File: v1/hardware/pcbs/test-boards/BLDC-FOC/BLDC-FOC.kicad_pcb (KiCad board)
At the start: 2 copper layers, 100 x 100 mm, 83 parts, among them CN1 HB9500-3, Q1 BSC190N15NS3G(TOKMAS), Q2 BSC190N15NS3G(TOKMAS), Q3 BSC190N15NS3G(TOKMAS), Q4 BSC190N15NS3G(TOKMAS), Q5 BSC190N15NS3G(TOKMAS), Q6 BSC190N15NS3G(TOKMAS)

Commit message: bldc foc test board done
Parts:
- removed BUCK1: LM5164DDA, Package_SO:HSOP-8-1EP_3.9x4.9mm_P1.27mm_EP2.41x3.1mm
- removed L1: PSPMAA0605H-820M-IGF, EasyEDA:IND-SMD_L7.1-W6.6
- added C37: 1uF 200V, Capacitor_SMD:C_1812_4532Metric, F.Cu at (-13.2, 26.1)
- added C38: 1uF 200V, Capacitor_SMD:C_1812_4532Metric, F.Cu at (-38.2, 36.2)
- added C39: 100nF, Capacitor_SMD:C_0603_1608Metric, F.Cu at (-28.0, 5.00)
- added C40: 100nF, Capacitor_SMD:C_0603_1608Metric, F.Cu at (-35.8, 1.00)
- added C41: 4.7nF, Capacitor_SMD:C_0603_1608Metric, F.Cu at (-32.2, -3.60)
- added C5: 1uF 200V, Capacitor_SMD:C_1812_4532Metric, F.Cu at (-21.6, 18.9)
- added C6: 1uF 200V, Capacitor_SMD:C_1812_4532Metric, F.Cu at (-45.8, 36.2)
- added C7: 10uF 25V, Capacitor_SMD:C_0603_1608Metric, F.Cu at (-38.2, 31.6)
- added C8: 100nF 25V, Capacitor_SMD:C_0603_1608Metric, F.Cu at (-35.2, 26.6)
- added D4: SMAJ85CA, Diode_SMD:D_SMA, F.Cu at (-21.6, 22.7)
- added D5: SMAJ15CA, Diode_SMD:D_SMA, F.Cu at (-42.0, 35.6)
- added F1: R1245.100, EasyEDA:FUSE-SMD_L12.5-W4.5, F.Cu at (-14.4, 5.50)
- added J1: Conn_01x12, Connector_JST:JST_XH_S12B-XH-A_1x12_P2.50mm_Horizontal, F.Cu at (-40.0, -4.50)
- added J2: Conn_01x10, Connector_JST:JST_XH_S10B-XH-A_1x10_P2.50mm_Horizontal, F.Cu at (40.0, -20.0)
- added J3: Conn_02x02_Odd_Even, Connector_PinHeader_2.54mm:PinHeader_2x02_P2.54mm_Vertical, F.Cu at (-26.9, -2.33)
- added JP1: Jumper_3_Bridged12, Connector_PinHeader_2.54mm:PinHeader_1x03_P2.54mm_Vertical, F.Cu at (-8.54, -39.0)
- added L2: SL0420-4R7M, EasyEDA:IND-SMD_L4.5-W4.1_IHLP, F.Cu at (-31.4, 26.0)
- added P1: WJ500V-5.08-2P-14-00A, EasyEDA:CONN-TH_2P-P5.00_WJ500V-5.08-2P, F.Cu at (-41.0, 44.0)
- added Q7: SP015N03BGHTO, EasyEDA:TOLL-8_L10.4-W9.9-P1.20-LS11.7-BL, F.Cu at (-12.8, 19.2)
- added Q8: AO3400A_C347475, EasyEDA:SOT-23-3_L2.9-W1.3-P1.90-LS2.4-BR, F.Cu at (-42.6, 28.6)
- added R35: 60, Resistor_SMD:R_0603_1608Metric, F.Cu at (-28.2, -7.60)
- added R36: 60, Resistor_SMD:R_0603_1608Metric, F.Cu at (-28.2, 0.40)
- added R37: 2.7K, Resistor_SMD:R_0603_1608Metric, F.Cu at (-40.3, -44.5)
- added R38: 2.7K, Resistor_SMD:R_0603_1608Metric, F.Cu at (-37.1, -44.5)
- added R39: 2.7K, Resistor_SMD:R_0603_1608Metric, F.Cu at (2.00, -47.3)
- added R40: 2.7K, Resistor_SMD:R_0603_1608Metric, F.Cu at (0.80, -46.1)
- added TP1: TestPoint, Connector_PinSocket_2.54mm:PinSocket_1x01_P2.54mm_Vertical, F.Cu at (36.6, -13.4)
- added TP17: TestPoint, Connector_PinSocket_2.54mm:PinSocket_1x01_P2.54mm_Vertical, F.Cu at (-34.2, -9.20)
- added TP2: TestPoint, Connector_PinSocket_2.54mm:PinSocket_1x01_P2.54mm_Vertical, F.Cu at (32.0, 4.20)
- added TP3: TestPoint, Connector_PinSocket_2.54mm:PinSocket_1x01_P2.54mm_Vertical, F.Cu at (36.6, 27.0)
- added TP4: TestPoint, Connector_PinSocket_2.54mm:PinSocket_1x01_P2.54mm_Vertical, F.Cu at (29.6, -26.8)
- added TP5: TestPoint, Connector_PinSocket_2.54mm:PinSocket_1x01_P2.54mm_Vertical, F.Cu at (-48.0, 45.0)
- added TP6: TestPoint, Connector_PinSocket_2.54mm:PinSocket_1x01_P2.54mm_Vertical, F.Cu at (-8.80, -7.60)
- added TP7: TestPoint, Connector_PinSocket_2.54mm:PinSocket_1x01_P2.54mm_Vertical, F.Cu at (-3.00, -29.4)
- added U2: MX74700T_C22468156, EasyEDA:SOT-23-6_L2.9-W1.6-P0.95-LS2.9-BL, F.Cu at (-21.6, 15.1)
- added U3: KF88SA-16.0-2P, EasyEDA:CONN-TH_KF88SA-16.0-2P, F.Cu at (-17.0, 39.0)
- added U4: MX74700T_C22468156, EasyEDA:SOT-23-6_L2.9-W1.6-P0.95-LS2.9-BL, F.Cu at (-46.0, 30.6)
- added U5: AP63205WU, Package_TO_SOT_SMD:TSOT-23-6, F.Cu at (-38.2, 29.0)
- added U6: AZ1117EH-3.3TRG1, EasyEDA:SOT-223_L6.5-W3.5-P2.30-LS7.0-BR, F.Cu at (-28.4, 12.6)
- added U7: TXS0108EPW, Package_SO:TSSOP-20_4.4x6.5mm_P0.65mm, F.Cu at (-6.00, -45.0)
- added U8: TCAN1057AVDRQ1, EasyEDA:SOIC-8_L4.9-W3.9-P1.27-LS6.0-BL, F.Cu at (-33.0, 5.00)
- C12: value 22uF 100V -> 22uF 25V; footprint Capacitor_SMD:C_Elec_6.3x7.7 -> Capacitor_SMD:C_0805_2012Metric
- C13: value 2.2uF 100V -> 22uF 25V; footprint Capacitor_SMD:C_1210_3225Metric -> Capacitor_SMD:C_0805_2012Metric
- C14: value 2.2nF 50V X7R -> 1uF
- C15: value 47uF 50V -> 1uF; footprint Capacitor_SMD:C_Elec_6.3x7.7 -> Capacitor_SMD:C_0603_1608Metric
- Q1, Q2, Q3, Q4, Q5, Q6: value BSC190N15NS3G(TOKMAS) -> BSC093N15NS5
- R4: value 124K -> 32.4K
- R6: value 448K -> 32.4K
- R7: value 39K -> 10K
- moved C2 166.0 mm to (11.3, -35.2), turned to 180 degrees
- moved C4 153.4 mm to (5.75, 19.2), turned to 180 degrees
- moved C3 153.0 mm to (5.75, 0.40), turned to 180 degrees
- moved C1 140.2 mm to (3.15, -18.2), turned to 180 degrees
- moved C10 133.8 mm to (26.0, -40.0)
- moved C11 133.8 mm to (24.6, -36.2)
- moved C9 133.8 mm to (24.6, -43.8)
- moved D1 133.8 mm to (22.2, -46.0)
- moved D2 133.8 mm to (28.2, -42.4)
- moved D3 133.8 mm to (27.0, -34.0)
- moved GDRV1 133.8 mm to (22.0, -40.0)
- moved R1 107.5 mm to (-11.2, -13.8), turned to 180 degrees
- moved R2 104.7 mm to (-12.0, -16.2), turned to 90 degrees
- moved R3 103.1 mm to (-12.0, -19.4), turned to 90 degrees
- moved C15 99.1 mm to (-25.6, 9.60), turned to 90 degrees
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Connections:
- C12 pad 1: VMOT -> +5V
- C13 pad 1: VMOT -> +5V
- C14 pad 1: Net-(BUCK1-BST) -> +5V
- C14 pad 2: Net-(BUCK1-SW) -> GND
- C15 pad 1: VGATE -> +3V3
- D1 pad 2: VGATE -> +12V
- D2 pad 2: VGATE -> +12V
- D3 pad 2: VGATE -> +12V
- GDRV1 pad 4: VGATE -> +12V
- R4 pad 1: Net-(BUCK1-RON) -> +5V
- R4 pad 2: GND -> /5V_SENSE
- R5 pad 1: /BUCK_PGOOD -> /5V_SENSE
- R5 pad 2: +3V3 -> GND
- R6 pad 1: VGATE -> +12V
- R6 pad 2: Net-(BUCK1-FB) -> /12V_SENSE
- R7 pad 1: Net-(BUCK1-FB) -> /12V_SENSE
- U1 pad 10: unconnected-(U1-PB7-Pad10) -> /USART1_RX
- U1 pad 12: unconnected-(U1-PC13-Pad12) -> /U_LOW_PWM
- U1 pad 13: unconnected-(U1-PA0-Pad13) -> /VMOT_SENSE
- U1 pad 14: unconnected-(U1-NRST-Pad14) -> /NRST
- U1 pad 15: /SK6812_data -> unconnected-(U1-SK6812_data-Pad15)
- U1 pad 16: +3V3 -> unconnected-(U1-3V3-Pad16)
- U1 pad 23: unconnected-(U1-PA9-Pad23) -> /V_HIGH_PWM
- U1 pad 24: unconnected-(U1-PA8-Pad24) -> /U_HIGH_PWM
- U1 pad 25: unconnected-(U1-PB14-Pad25) -> /V_LOW_PWM
- U1 pad 26: unconnected-(U1-PB13-Pad26) -> /FDCAN2_TX
- U1 pad 27: unconnected-(U1-PB12-Pad27) -> /FDCAN2_RX
- U1 pad 28: unconnected-(U1-PB11-Pad28) -> /SHIFTER_OE
- U1 pad 29: unconnected-(U1-PB2-Pad29) -> /CAN_SILENT
- U1 pad 3: unconnected-(U1-PA10-Pad3) -> /W_HIGH_PWM
- U1 pad 30: unconnected-(U1-PB1-Pad30) -> /W_LOW_PWM
- U1 pad 31: unconnected-(U1-PB0-Pad31) -> /V_I_SENSE
- U1 pad 32: unconnected-(U1-PA7-Pad32) -> /W_I_SENSE
- U1 pad 33: unconnected-(U1-PA6-Pad33) -> /12V_SENSE
- U1 pad 34: unconnected-(U1-PA5-Pad34) -> /5V_SENSE
- U1 pad 35: unconnected-(U1-PA4-Pad35) -> /SPI1_SCS
- U1 pad 36: unconnected-(U1-PA3-Pad36) -> /USART2_RX
- U1 pad 37: GND -> /USART2_TX
- U1 pad 38: +5V -> /U_I_SENSE
- U1 pad 4: unconnected-(U1-PB9-Pad4) -> /I2C1_SDA
- U1 pad 41: (no net) -> unconnected-(U1-H1-Pad41)_2
- U1 pad 42: (no net) -> unconnected-(U1-H2-Pad42)_2
- U1 pad 43: (no net) -> unconnected-(U1-H3-Pad43)_4
- U1 pad 5: unconnected-(U1-PA15-Pad5) -> /I2C1_SCL
- U1 pad 6: unconnected-(U1-PB3-Pad6) -> /SPI1_SCLK
- U1 pad 7: unconnected-(U1-PB4-Pad7) -> /SPI1_MISO
- U1 pad 8: unconnected-(U1-PB5-Pad8) -> /SPI1_MOSI
- U1 pad 9: unconnected-(U1-PB6-Pad9) -> /USART1_TX
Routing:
- net +5V: track 0.00 -> 223.3 mm
- net +12V: track 0.00 -> 186.8 mm, vias 0 -> 12
- net /W_I_SENSE: track 4.49 -> 123.7 mm, vias 0 -> 1
- net /V_I_SENSE: track 4.49 -> 93.6 mm, vias 0 -> 1
- net /U_LOW_PWM: track 2.00 -> 85.6 mm, vias 0 -> 1
- net ENC_VCC: track 0.00 -> 79.8 mm
- net /W_HIGH_PWM: track 2.66 -> 81.6 mm, vias 0 -> 2
- net +3V3: track 14.5 -> 89.1 mm, vias 0 -> 23
- net /U_I_SENSE: track 4.49 -> 72.5 mm, vias 0 -> 1
- net /W_LOW_GATE: track 12.8 -> 80.6 mm, vias 0 -> 2
- net GND: track 168.2 -> 234.5 mm, vias 132 -> 147
- net /W_HIGH_GATE: track 20.3 -> 79.9 mm, vias 0 -> 2
- net /USART1_RX_ENC: track 0.00 -> 58.7 mm, vias 0 -> 1
- net /USART1_TX_ENC: track 0.00 -> 56.8 mm, vias 0 -> 1
- net /SPI1_SCS_ENC: track 0.00 -> 54.6 mm, vias 0 -> 1
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- added copper zone on In1.Cu, net +3V3
- added copper zone on F.Cu, net /power/VMOT_UNFILTERED
- added copper zone on F.Cu, net /power/VMOT_UNFUSED
- added copper zone on In2.Cu, net GND
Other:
- outline, holes or cut-outs redrawn
- copper layers 2 -> 4
- board text added: "100nF 25V"
- board text added: "10uF 25V"
- board text added: "12V GND"
- board text added: "1uF"
- board text added: "2.7K"
- board text added: "22uF 25V"
- board text added: "32.4K"
- board text added: "3PHASE POWER"
- board text added: "3V3"
- board text added: "4.7nF"
- board text added: "5V"
- board text added: "60"
- board text added: "AO3400A"
- board text added: "AP63205WU"
- board text added: "AZ1117EH -3.3TRG1"
- board text added: "BOOT0"
- board text added: "CAN +"
- board text added: "CAN -"
- board text added: "CAN+"
- board text added: "CAN-"
- board text added: "CAN_TERM"
- board text added: "ENCODER"
- board text added: "ENC_VCC"
- board text added: "GND"
- board text added: "KF88SA-16.0-2P"
- board text added: "MISO/GP"
- board text added: "MOSI/GP"
- board text added: "MX74700T"
- board text added: "NRST"
- board text added: "R1245.100"
- board text added: "RX/GP"
- board text added: "SCL"
- board text added: "SCLK/GP"
- board text added: "SCS/GP"
- board text added: "SDA"
- board text added: "SL0420 -4R7M"
- board text added: "SMAJ85CA"
- board text added: "SP015N03BGHTO"
- board text added: "TCAN1057AVDRQ1"
- board text added: "TX/GP"
- board text added: "TXS0108EPW"
- board text added: "U"
- board text added: "UART_RX"
- board text added: "UART_TX"
- board text added: "V"
- board text added: "VMOT"
- board text added: "W"
- board text added: "WJ500V-5.08 -2P-14-00A"
- board text removed: "124K"
- board text removed: "2.2nF 50V X7R"
- board text removed: "2.2uF 100V"
- board text removed: "22uF 100V"
- board text removed: "39K"
- board text removed: "448K"
- board text removed: "47uF 50V"
- board text removed: "82uH I_sat >= 1.6A PSPMAA0605H -820M-IGF"
- board text removed: "LM5164DDA"

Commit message: flooded ground
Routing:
- added copper zone on B.Cu, net GND
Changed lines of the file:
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@@
+	)
+	(zone
+		(net 71)
+		(net_name "GND")
+		(layers "F.Cu" "B.Cu" "In2.Cu")
+		(hatch edge 0.5)
+		(connect_pads yes
+			(clearance 0.5)
+		)
+		(min_thickness 0.25)
+		(filled_areas_thickness no)
+		(fill yes
+			(thermal_gap 0.5)
+			(thermal_bridge_width 0.5)
+		)
+		(polygon
+			(pts
+				(xy -51 -51) (xy 51 -51) (xy 51 51) (xy -51 51)
+			)
+		)
 	)
 	(zone
@@
 			)
 		)
-	)
-	(zone
-		(net 71)
-		(net_name "GND")
-		(layer "In2.Cu")
-		(hatch edge 0.5)
-		(priority 1)
-		(connect_pads yes
-			(clearance 0.5)
-		)
-		(min_thickness 0.25)
-		(filled_areas_thickness no)
-		(fill yes
-			(thermal_gap 0.5)
-			(thermal_bridge_width 0.5)
-		)
-		(polygon
-			(pts
-				(xy -51 -51) (xy 51 -51) (xy 51 51) (xy -51 51)
-			)
-		)

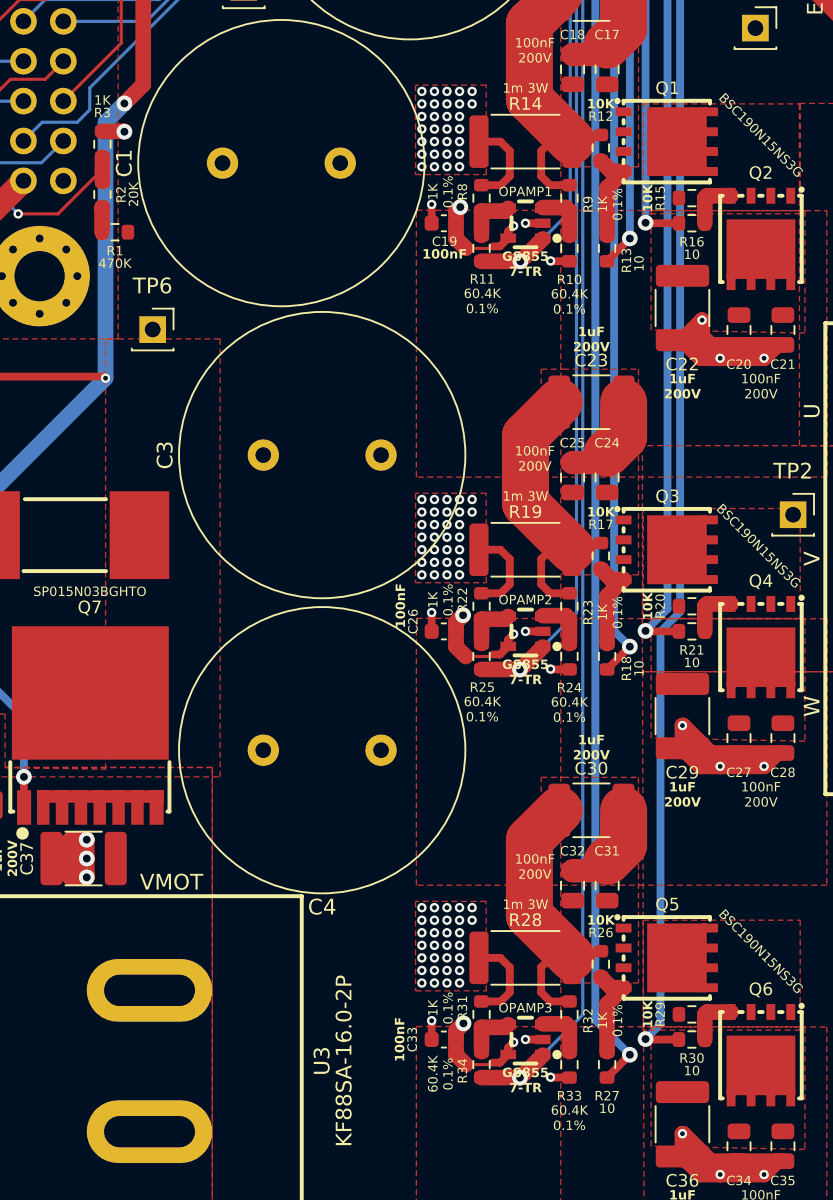
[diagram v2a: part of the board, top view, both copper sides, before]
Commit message: larger resistors for high voltages, new prod files
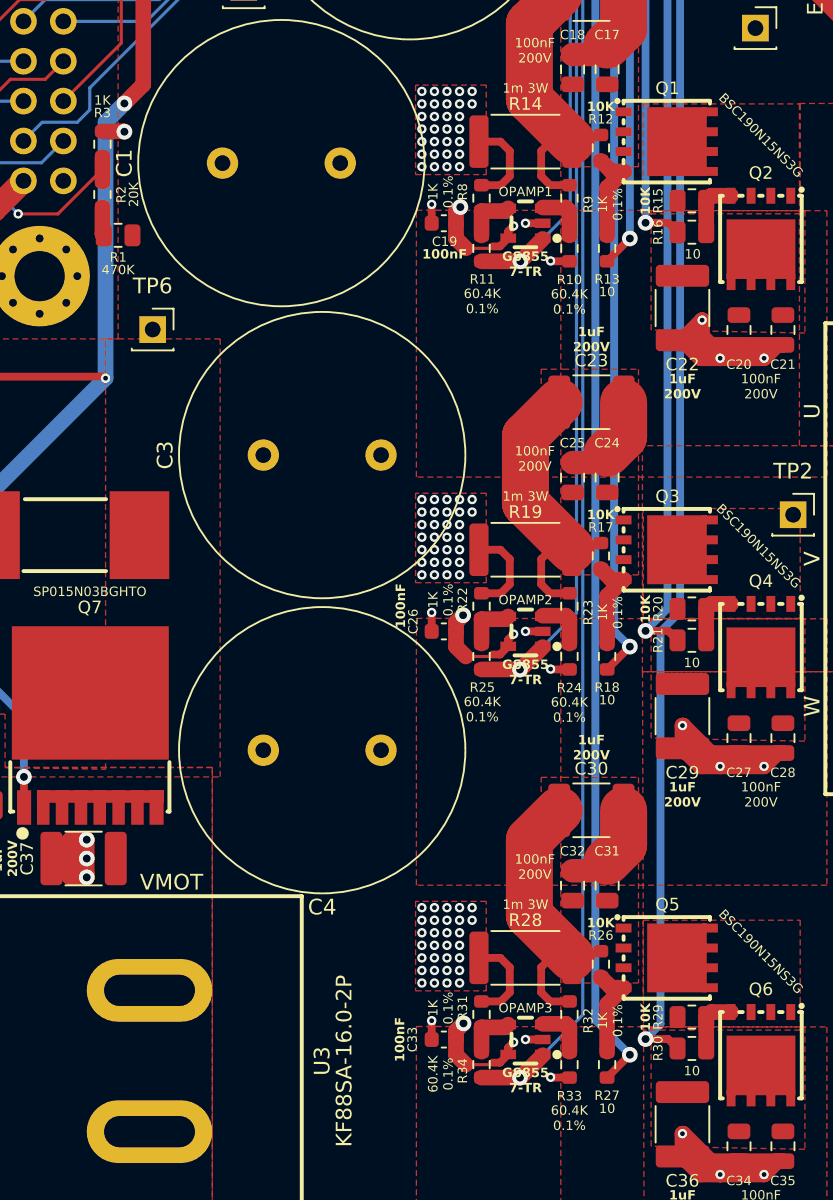
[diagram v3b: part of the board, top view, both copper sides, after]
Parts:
- C1, C2, C3, C4: value 470uF 100V (C443161) -> 820uF 100V (C443165)
- R1, R15, R16, R20, R21, R29, R30: footprint Resistor_SMD:R_0603_1608Metric -> Resistor_SMD:R_0805_2012Metric
- moved R16 0.57 mm to (25.6, -13.8)
- moved R30 0.57 mm to (25.6, 38.2)
- moved R21 0.57 mm to (25.6, 12.2)
- moved R1 0.28 mm to (-11.0, -13.6)
- moved R15 0.17 mm to (25.6, -15.8)
- moved R29 0.17 mm to (25.6, 36.2)
- moved R20 0.17 mm to (25.6, 10.2)

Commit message: new FOC driver schematic
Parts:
- C1, C2, C3, C4: footprint Capacitor_THT:C_Radial_D18.0mm_H35.5mm_P7.50mm -> footprints:C_Radial_D18.0mm_H35.5mm_P7.50mm
- C10, C11, C12, C13, C17, C18, C20, C21, C24, C25, C27, C28, C31, C32, C34, C35, C9: footprint Capacitor_SMD:C_0805_2012Metric -> footprints:C_0805_2012Metric
- C14, C15, C19, C26, C33, C39, C40, C41, C7, C8: footprint Capacitor_SMD:C_0603_1608Metric -> footprints:C_0603_1608Metric
- C16, C22, C23, C29, C30, C36, C37, C38, C5, C6: footprint Capacitor_SMD:C_1812_4532Metric -> footprints:C_1812_4532Metric
- CN1: footprint EasyEDA:CONN-TH_3P-P9.50_HB9500-9.5-3P -> footprints:CONN-TH_3P-P9.50_HB9500-9.5-3P
- D1, D2, D3: value B5819W -> C7420332; footprint Diode_SMD:D_SOD-123F -> footprints:D_SOD-123F
- D4, D5: footprint Diode_SMD:D_SMA -> footprints:D_SMA
- F1: footprint EasyEDA:FUSE-SMD_L12.5-W4.5 -> footprints:FUSE-SMD_L12.5-W4.5
- GDRV1: footprint Snapeda:FD6288Q_QFN50P400X400X90-25N -> footprints:FD6288Q_QFN50P400X400X90-25N
- J1: footprint Connector_JST:JST_XH_S12B-XH-A_1x12_P2.50mm_Horizontal -> footprints:JST_XH_S12B-XH-A_1x12_P2.50mm_Horizontal
- J2: footprint Connector_JST:JST_XH_S10B-XH-A_1x10_P2.50mm_Horizontal -> footprints:JST_XH_S10B-XH-A_1x10_P2.50mm_Horizontal
- J3: footprint Connector_PinHeader_2.54mm:PinHeader_2x02_P2.54mm_Vertical -> footprints:PinHeader_2x02_P2.54mm_Vertical
- JP1: footprint Connector_PinHeader_2.54mm:PinHeader_1x03_P2.54mm_Vertical -> footprints:PinHeader_1x03_P2.54mm_Vertical
- L2: footprint EasyEDA:IND-SMD_L4.5-W4.1_IHLP -> footprints:IND-SMD_L4.5-W4.1_IHLP
- OPAMP1, OPAMP2, OPAMP3: footprint EasyEDA:SOT-23-5_L2.9-W1.6-P0.95-LS2.8-BR -> footprints:SOT-23-5_L2.9-W1.6-P0.95-LS2.8-BR
- P1: footprint EasyEDA:CONN-TH_2P-P5.00_WJ500V-5.08-2P -> footprints:CONN-TH_2P-P5.00_WJ500V-5.08-2P
- Q1, Q2, Q3, Q4, Q5, Q6: footprint EasyEDA:DFN-8_L5.5-W5.2-P1.27-LS6.1-BL -> footprints:DFN-8_L5.5-W5.2-P1.27-LS6.1-BL
- Q7: footprint EasyEDA:TOLL-8_L10.4-W9.9-P1.20-LS11.7-BL -> footprints:TOLL-8_L10.4-W9.9-P1.20-LS11.7-BL
- Q8: footprint EasyEDA:SOT-23-3_L2.9-W1.3-P1.90-LS2.4-BR -> footprints:SOT-23-3_L2.9-W1.3-P1.90-LS2.4-BR
- R1: value 470K -> 47K; footprint Resistor_SMD:R_0805_2012Metric -> footprints:R_0805_2012Metric
- R10, R11, R12, R13, R17, R18, R22, R23, R24, R25, R26, R27, R3, R31, R32, R33, R34, R37, R38, R39, R4, R40, R5, R6, R7, R8, R9: footprint Resistor_SMD:R_0603_1608Metric -> footprints:R_0603_1608Metric
- R14, R19, R28: footprint Resistor_SMD:R_2512_6332Metric -> footprints:R_2512_6332Metric
- R15, R16, R20, R21, R29, R30: footprint Resistor_SMD:R_0805_2012Metric -> footprints:R_0805_2012Metric
- R2: value 20K -> 2K; footprint Resistor_SMD:R_0603_1608Metric -> footprints:R_0603_1608Metric
- R35, R36: value 60 -> 60.4; footprint Resistor_SMD:R_0603_1608Metric -> footprints:R_0603_1608Metric
- TP1, TP17, TP2, TP3, TP4, TP5, TP6, TP7: footprint Connector_PinSocket_2.54mm:PinSocket_1x01_P2.54mm_Vertical -> footprints:PinSocket_1x01_P2.54mm_Vertical
- U1: footprint Custom:STM32G491CET6 breakout -> footprints:STM32G491CET6 breakout
- U2, U4: footprint EasyEDA:SOT-23-6_L2.9-W1.6-P0.95-LS2.9-BL -> footprints:SOT-23-6_L2.9-W1.6-P0.95-LS2.9-BL
- U3: footprint EasyEDA:CONN-TH_KF88SA-16.0-2P -> footprints:CONN-TH_KF88SA-16.0-2P
- U5: footprint Package_TO_SOT_SMD:TSOT-23-6 -> footprints:TSOT-23-6
- U6: footprint EasyEDA:SOT-223_L6.5-W3.5-P2.30-LS7.0-BR -> footprints:SOT-223_L6.5-W3.5-P2.30-LS7.0-BR
- U7: footprint Package_SO:TSSOP-20_4.4x6.5mm_P0.65mm -> footprints:TSSOP-20_4.4x6.5mm_P0.65mm
- U8: footprint EasyEDA:SOIC-8_L4.9-W3.9-P1.27-LS6.0-BL -> footprints:SOIC-8_L4.9-W3.9-P1.27-LS6.0-BL
